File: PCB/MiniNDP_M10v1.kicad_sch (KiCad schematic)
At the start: 14 parts, among them J1 Conn_02x20_Odd_Even, U1 AS6C8008_TSOPII, U2 HC238, U3 HC4040, U4 ABT841

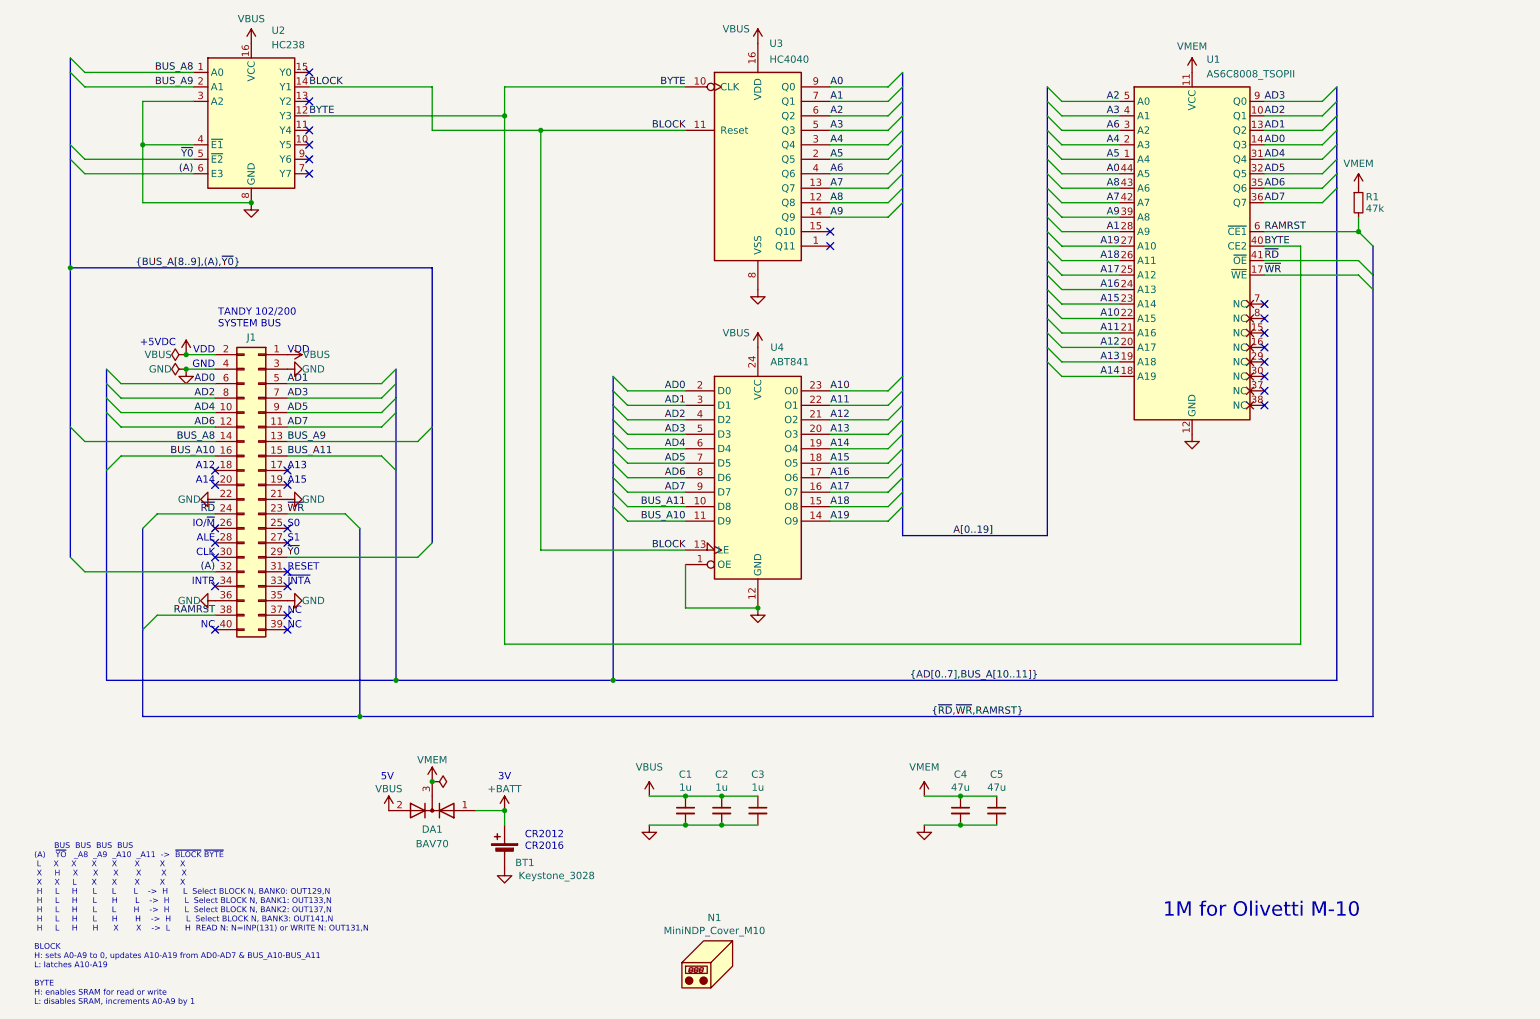
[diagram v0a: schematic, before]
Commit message: Olivetti M-10 take 3. T512 pics readme.
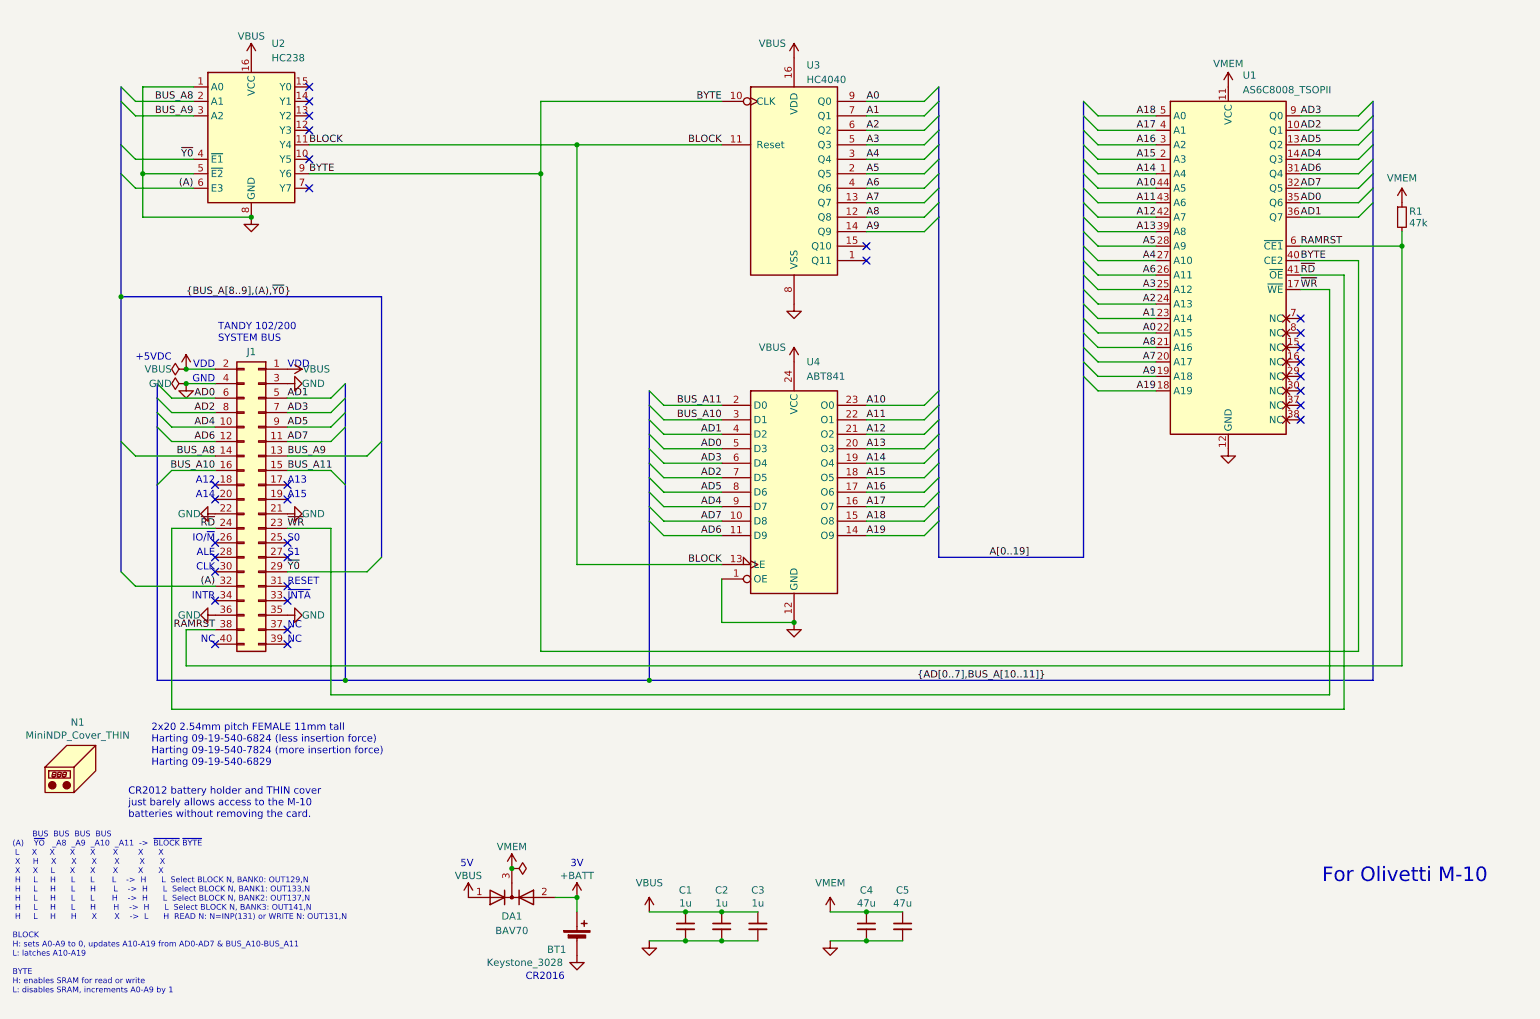
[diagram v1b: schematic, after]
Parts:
- J1: footprint 000_LOCAL:PinSocket_2x20_P2.54mm_Vertical -> 000_LOCAL:Harting_09-19-540-x824; MPN ESW-120-12-L-D -> 09-19-540-7824
- N1: value MiniNDP_Cover_M10 -> MiniNDP_Cover_THIN; footprint 000_LOCAL:MiniNDP_Cover_M10 -> 000_LOCAL:MiniNDP_Cover_THIN; MPN MiniNDP_Cover_M10.stl -> MiniNDP_Cover_THIN.stl
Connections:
- net +BATT: now also DA1.2 (A); no longer DA1.1 (A)
- net A0: now also U1.22 (A15); no longer U1.44 (A5)
- net A1: now also U1.23 (A14); no longer U1.28 (A9)
- net A10: now also U1.44 (A5); no longer U1.22 (A15)
- net A11: now also U1.43 (A6); no longer U1.21 (A16)
- net A12: now also U1.42 (A7); no longer U1.20 (A17)
- net A13: now also U1.39 (A8); no longer U1.19 (A18)
- net A14: now also U1.1 (A4); no longer U1.18 (A19)
- net A15: now also U1.2 (A3); no longer U1.23 (A14)
- net A16: now also U1.3 (A2); no longer U1.24 (A13)
- net A17: now also U1.4 (A1); no longer U1.25 (A12)
- net A18: now also U1.5 (A0); no longer U1.26 (A11)
- net A19: now also U1.18 (A19); no longer U1.27 (A10)
- net A2: now also U1.24 (A13); no longer U1.5 (A0)
- net A3: now also U1.25 (A12); no longer U1.4 (A1)
- net A4: now also U1.27 (A10); no longer U1.2 (A3)
- net A5: now also U1.28 (A9); no longer U1.1 (A4)
- net A6: now also U1.26 (A11); no longer U1.3 (A2)
- net A7: now also U1.20 (A17); no longer U1.42 (A7)
- net A8: now also U1.21 (A16); no longer U1.43 (A6)
- net A9: now also U1.19 (A18); no longer U1.39 (A8)
- net AD0: now also U1.35 (Q6), U4.5 (D3); no longer U1.14 (Q3), U4.2 (D0)
- net AD1: now also U1.36 (Q7), U4.4 (D2); no longer U1.13 (Q2), U4.3 (D1)
- net AD2: now also U4.7 (D5); no longer U4.4 (D2)
- net AD3: now also U4.6 (D4); no longer U4.5 (D3)
- net AD4: now also U1.14 (Q3), U4.9 (D7); no longer U1.31 (Q4), U4.6 (D4)
- net AD5: now also U1.13 (Q2), U4.8 (D6); no longer U1.32 (Q5), U4.7 (D5)
- net AD6: now also U1.31 (Q4), U4.11 (D9); no longer U1.35 (Q6), U4.8 (D6)
- net AD7: now also U1.32 (Q5), U4.10 (D8); no longer U1.36 (Q7), U4.9 (D7)
- net BLOCK: now also U2.11 (Y4); no longer U2.14 (Y1)
- net BUS_A10: now also U4.3 (D1); no longer U4.11 (D9)
- net BUS_A11: now also U4.2 (D0); no longer U4.10 (D8)
- net BUS_A8: now also U2.2 (A1); no longer U2.1 (A0)
- net BUS_A9: now also U2.3 (A2); no longer U2.2 (A1)
- net BYTE: now also U2.9 (Y6); no longer U2.12 (Y3)
- net GND: now also U2.1 (A0), U2.5 (~{E2}); no longer U2.3 (A2), U2.4 (~{E1})
- net VBUS: now also DA1.1 (A); no longer DA1.2 (A)
- net ~{Y0}: now also U2.4 (~{E1}); no longer U2.5 (~{E2})
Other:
- note added: "2x20 2.54mm pitch FEMALE 11mm tall Harting 09-19-540-6824 (less insertion force) Harting 09-19-540-7824 (more insertion force) Harting 09-19-540-6829"
- note added: "CR2012 battery holder and THIN cover just barely allows access to the M-10 batteries without removing the card."
- note added: "CR2016"
- note added: "For Olivetti M-10"
- note removed: "1M for Olivetti M-10"
- note removed: "CR2012 CR2016"
- moved on the sheet: C1, C2, C3, C5, DA1, J1, N1, R1, U1, U2, U3, U4
